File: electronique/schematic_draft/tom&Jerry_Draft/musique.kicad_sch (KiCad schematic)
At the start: 10 parts, among them U601 PAM8302AAY

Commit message: KiCAD V3 - 18.09.2024
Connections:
- net DAC STM32 renamed DAC_STM+
- net DAC_STM+: no longer C604.1
- new net DAC_STM-: C604.1
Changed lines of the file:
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@@
 		)
 	)
-	(global_label "HP+"
+	(hierarchical_label "HP+"
 		(shape input)
 		(at 167.64 81.28 0)
@@
 			(justify left)
 		)
-		(property "Intersheetrefs" "${INTERSHEET_REFS}"
-			(at 174.7981 81.28 0)
-			(effects
-				(font
-					(size 1.27 1.27)
-				)
-				(justify left)
-				(hide yes)
+	)
+	(hierarchical_label "HP-"
+		(shape input)
+		(at 167.64 99.06 0)
+		(fields_autoplaced yes)
+		(effects
+			(font
+				(size 1.27 1.27)
 			)
+			(justify left)
 		)
 	)
-	(global_label "DAC STM32"
+	(hierarchical_label "DAC_STM+"
 		(shape input)
 		(at 110.49 86.36 180)
@@
 			(justify right)
 		)
-		(property "Intersheetrefs" "${INTERSHEET_REFS}"
-			(at 96.8611 86.36 0)
-			(effects
-				(font
-					(size 1.27 1.27)
-				)
-				(justify right)
-				(hide yes)
-			)
-		)
 	)
-	(global_label "HP-"
-		(shape input)
-		(at 167.64 99.06 0)
-		(fields_autoplaced yes)
-		(effects
-			(font
-				(size 1.27 1.27)
-			)
-			(justify left)
-		)
-		(property "Intersheetrefs" "${INTERSHEET_REFS}"
-			(at 174.7981 99.06 0)
-			(effects
-				(font
-					(size 1.27 1.27)
-				)
-				(justify left)
-				(hide yes)
-			)
-		)
-	)
-	(global_label "DAC STM32"
+	(hierarchical_label "DAC_STM-"
 		(shape input)
 		(at 110.49 91.44 180)
@@
 			(justify right)
 		)
-		(property "Intersheetrefs" "${INTERSHEET_REFS}"
-			(at 96.8611 91.44 0)
-			(effects
-				(font
-					(size 1.27 1.27)
-				)
-				(justify right)
-				(hide yes)
-			)
-		)
 	)

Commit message: STM32 KiCAD V5 - 20.09.2024
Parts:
- added J601: Conn_01x02, symbol Connector_Generic:Conn_01x02
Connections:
- net HP+: now also J601.1 (Pin_1)
- net HP-: now also J601.2 (Pin_2)
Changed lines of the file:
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@@
 	)
 	(junction
-		(at 165.1 99.06)
+		(at 165.1 100.33)
 		(diameter 0)
 		(color 0 0 0 0)
@@
 	(wire
 		(pts
-			(xy 165.1 81.28) (xy 167.64 81.28)
+			(xy 165.1 81.28) (xy 190.5 81.28)
+		)
+		(stroke
+			(width 0)
+			(type default)
+		)
+	)
+	(wire
+		(pts
+			(xy 190.5 88.9) (xy 190.5 100.33)
 		)
 		(stroke
@@
 	(wire
 		(pts
+			(xy 190.5 81.28) (xy 190.5 86.36)
+		)
+		(stroke
+			(width 0)
+			(type default)
+		)
+	)
+	(wire
+		(pts
 			(xy 110.49 96.52) (xy 120.65 96.52)
 		)
@@
 	(wire
 		(pts
-			(xy 165.1 99.06) (xy 167.64 99.06)
+			(xy 165.1 100.33) (xy 190.5 100.33)
 		)
 		(stroke
@@
 		)
 	)
-	(hierarchical_label "HP+"
-		(shape input)
-		(at 167.64 81.28 0)
+	(label "HP-"
+		(at 190.5 93.98 0)
 		(fields_autoplaced yes)
 		(effects
@@
 				(size 1.27 1.27)
 			)
-			(justify left)
-		)
-	)
-	(hierarchical_label "HP-"
-		(shape input)
-		(at 167.64 99.06 0)
+			(justify left bottom)
+		)
+	)
+	(label "HP+"
+		(at 190.5 83.82 0)
 		(fields_autoplaced yes)
 		(effects
@@
 				(size 1.27 1.27)
 			)
-			(justify left)
+			(justify left bottom)
 		)
 	)
@@
 					(unit 1)
 				)
+			)
+		)
+	)
+	(symbol
+		(lib_id "Connector_Generic:Conn_01x02")
+		(at 195.58 86.36 0)
+		(unit 1)
+		(exclude_from_sim no)
+		(in_bom yes)
+		(on_board yes)
+		(dnp no)
+		(fields_autoplaced yes)
+		(property "Reference" "J601"
+			(at 198.12 86.3599 0)
+			(effects
+				(font
+					(size 1.27 1.27)
+				)
+				(justify left)
+			)
+		)
+		(property "Value" "Conn_01x02"
+			(at 198.12 88.8999 0)
+			(effects
+				(font
+					(size 1.27 1.27)
+				)
+				(justify left)
+			)
+		)
+		(property "Footprint" ""
+			(at 195.58 86.36 0)
+			(effects
+				(font
+					(size 1.27 1.27)
+				)
+				(hide yes)
+			)
+		)
+		(property "Datasheet" "~"
+			(at 195.58 86.36 0)
+			(effects
+				(font
+					(size 1.27 1.27)
+				)
+				(hide yes)
+			)
+		)
+		(property "Description" "Generic connector, single row, 01x02, script generated (kicad-library-utils/schlib/autogen/connector/)"
+			(at 195.58 86.36 0)
+			(effects
+				(font
+					(size 1.27 1.27)
+				)
+				(hide yes)
+			)
+		)
+		(pin "1"
+		)
+		(pin "2"
+		)
+		(instances
+			(project "tom&Jerry_Draft"
+				(path "/d6e3fbeb-d028-494d-83bf-2e4a8b12578d/8f8d8816-c3bc-4641-b521-76532fa599d5"
+					(reference "J601")
+					(unit 1)
+				)

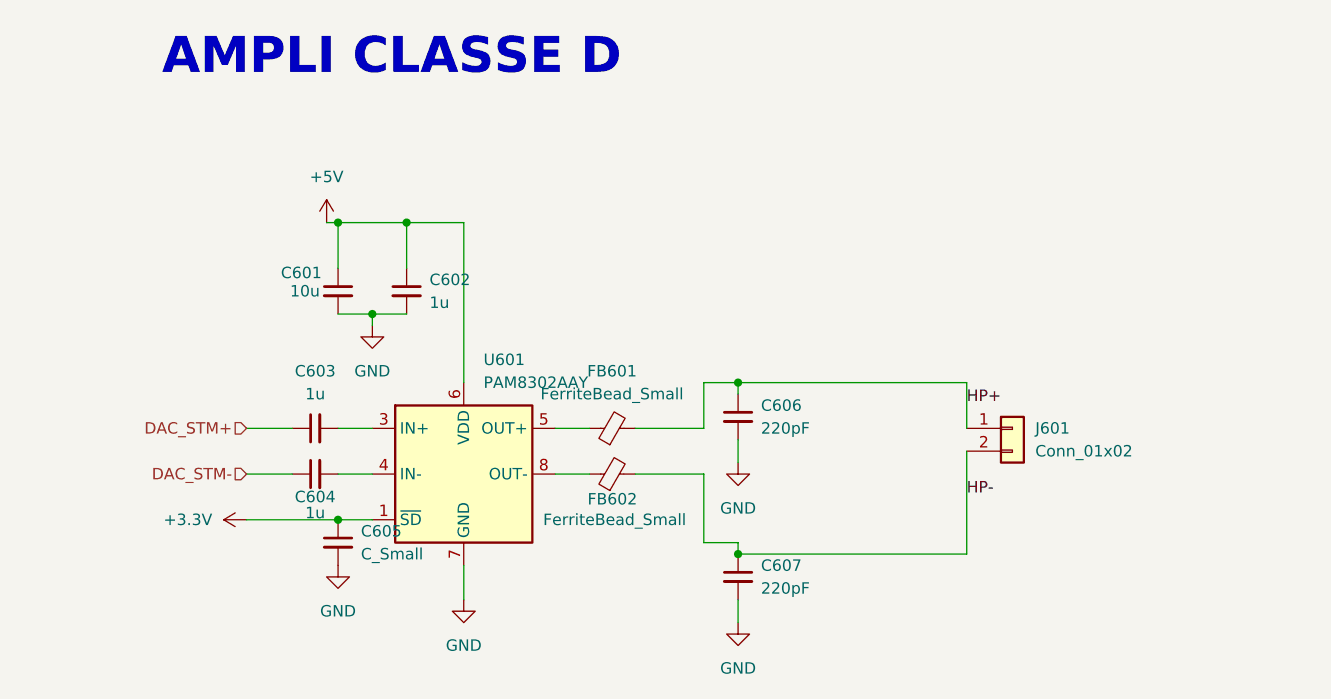
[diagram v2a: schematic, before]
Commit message: STM32 KiCAD V5 - 25.09.2024 - Ajout connecteurs TOF, ...
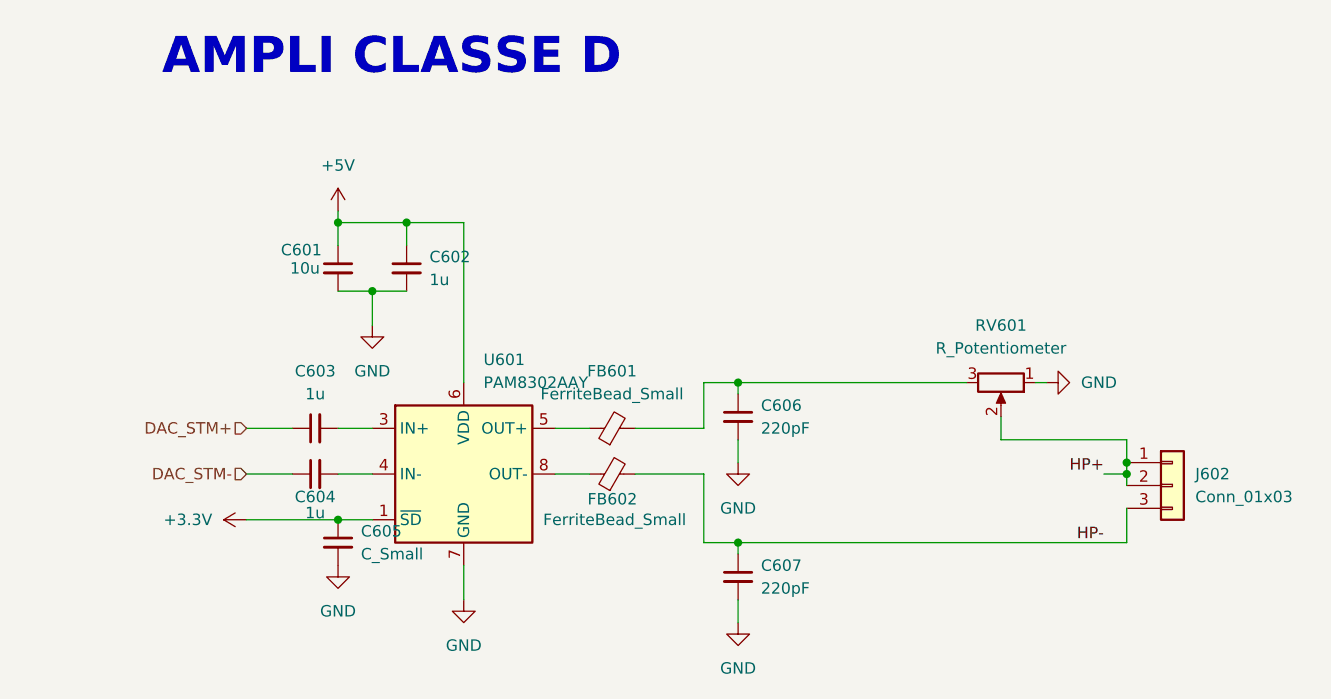
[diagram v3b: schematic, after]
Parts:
- removed J601: Conn_01x02, symbol Connector_Generic:Conn_01x02
- added J602: Conn_01x03, symbol Connector_Generic:Conn_01x03
- added RV601: R_Potentiometer, symbol Device:R_Potentiometer
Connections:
- net GND: now also RV601.1
- net HP+: now also J602.1 (Pin_1), J602.2 (Pin_2), RV601.2; no longer C606.1, FB601.2
- net HP-: now also J602.3 (Pin_3)
- new net: C606.1, FB601.2, RV601.3
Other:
- moved on the sheet: C601, C602

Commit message: STM32 KiCAD v2.0 x CubeIDE - Pin definitif + schematic reviewed
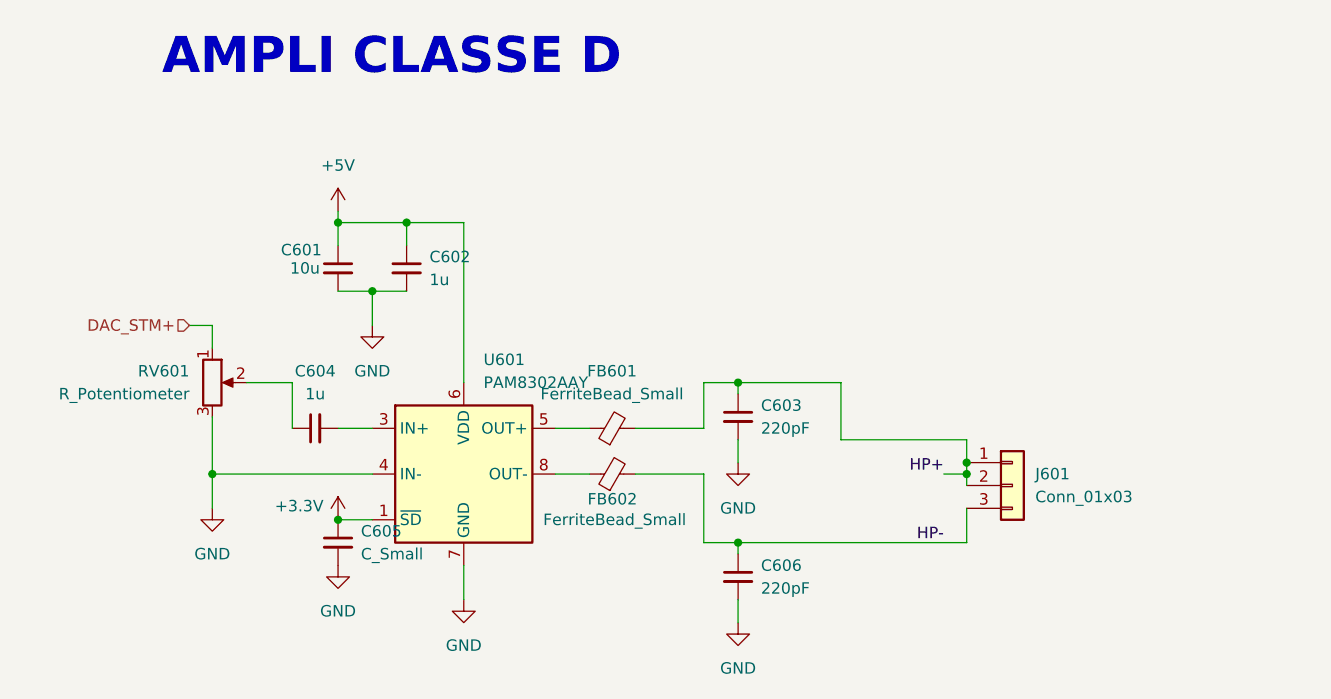
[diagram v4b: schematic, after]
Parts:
- removed C604: 1u, symbol Device:C_Small
- renumbered C606 to C603, C603 to C604, C607 to C606, J602 to J601
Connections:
- net DAC_STM+: now also RV601.1; no longer C604.1
- net GND: now also RV601.3, U601.4 (IN-); no longer RV601.1
- net HP+: now also C603.1, FB601.2; no longer RV601.2
- new net: C604.1, RV601.2
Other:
- moved on the sheet: J601

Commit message: Adding footprint V0.1
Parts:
- C601, C602, C604: footprint (none) -> Capacitor_SMD:C_0603_1608Metric
- C603, C606: value 220pF -> 220p; footprint (none) -> Capacitor_SMD:C_0402_1005Metric
- C605: value C_Small -> 100n; footprint (none) -> Capacitor_SMD:C_0402_1005Metric
- FB601, FB602: footprint (none) -> Inductor_SMD:L_0805_2012Metric
- J601: footprint (none) -> Connector_JST:JST_XH_S3B-XH-A_1x03_P2.50mm_Horizontal
- U601: footprint Package_DFN_QFN:DFN-8-1EP_3x3mm_P0.65mm_EP1.55x2.4mm -> Tom&Jerry:DFN300X300X80-8N
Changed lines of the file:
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@@
 			)
 		)
-		(property "Footprint" ""
+		(property "Footprint" "Capacitor_SMD:C_0603_1608Metric"
 			(at 118.11 86.36 0)
 			(effects
@@
 			)
 		)
-		(property "Value" "220pF"
+		(property "Value" "220p"
 			(at 167.64 104.1462 0)
 			(effects
@@
 			)
 		)
-		(property "Footprint" ""
+		(property "Footprint" "Capacitor_SMD:C_0402_1005Metric"
 			(at 165.1 102.87 0)
 			(effects
@@
 			)
 		)
-		(property "Value" "220pF"
+		(property "Value" "220p"
 			(at 167.64 86.3662 0)
 			(effects
@@
 			)
 		)
-		(property "Footprint" ""
+		(property "Footprint" "Capacitor_SMD:C_0402_1005Metric"
 			(at 165.1 85.09 0)
 			(effects
@@
 			)
 		)
-		(property "Footprint" ""
+		(property "Footprint" "Capacitor_SMD:C_0603_1608Metric"
 			(at 128.27 68.58 0)
 			(effects
@@
 			)
 		)
-		(property "Footprint" ""
+		(property "Footprint" "Connector_JST:JST_XH_S3B-XH-A_1x03_P2.50mm_Horizontal"
 			(at 195.58 92.71 0)
 			(effects
@@
 			)
 		)
-		(property "Footprint" "Package_DFN_QFN:DFN-8-1EP_3x3mm_P0.65mm_EP1.55x2.4mm"
+		(property "Footprint" "Tom&Jerry:DFN300X300X80-8N"
 			(at 134.62 91.44 0)
 			(effects
@@
 			)
 		)
-		(property "Footprint" ""
+		(property "Footprint" "Inductor_SMD:L_0805_2012Metric"
 			(at 151.13 88.138 90)
 			(effects
@@
 			)
 		)
-		(property "Footprint" ""
+		(property "Footprint" "Capacitor_SMD:C_0603_1608Metric"
 			(at 120.65 68.58 0)
 			(effects
@@
 			)
 		)
-		(property "Value" "C_Small"
+		(property "Value" "100n"
 			(at 123.19 100.3362 0)
 			(effects
@@
 			)
 		)
-		(property "Footprint" ""
+		(property "Footprint" "Capacitor_SMD:C_0402_1005Metric"
 			(at 120.65 99.06 0)
 			(effects
@@
 			)
 		)
-		(property "Footprint" ""
+		(property "Footprint" "Inductor_SMD:L_0805_2012Metric"
 			(at 151.13 93.218 90)
 			(effects

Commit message: Ajout V2 TOF + MultiPCB Panalize
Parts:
- renumbered C604 to C601, C601 to C602, C605 to C603, C602 to C604, C603 to C605
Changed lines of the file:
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@@
 		(dnp no)
 		(fields_autoplaced yes)
-		(property "Reference" "C604"
+		(property "Reference" "C601"
 			(at 118.1163 80.01 90)
 			(effects
@@
 			(project "tom&Jerry_Draft"
 				(path "/d6e3fbeb-d028-494d-83bf-2e4a8b12578d/8f8d8816-c3bc-4641-b521-76532fa599d5"
-					(reference "C604")
+					(reference "C601")
 					(unit 1)
 				)
@@
 		(dnp no)
 		(fields_autoplaced yes)
-		(property "Reference" "C603"
+		(property "Reference" "C605"
 			(at 167.64 83.8262 0)
 			(effects
@@
 			(project ""
 				(path "/d6e3fbeb-d028-494d-83bf-2e4a8b12578d/8f8d8816-c3bc-4641-b521-76532fa599d5"
-					(reference "C603")
+					(reference "C605")
 					(unit 1)
 				)
@@
 		(dnp no)
 		(fields_autoplaced yes)
-		(property "Reference" "C602"
+		(property "Reference" "C604"
 			(at 130.81 67.3162 0)
 			(effects
@@
 			(project "tom&Jerry_Draft"
 				(path "/d6e3fbeb-d028-494d-83bf-2e4a8b12578d/8f8d8816-c3bc-4641-b521-76532fa599d5"
-					(reference "C602")
+					(reference "C604")
 					(unit 1)
 				)
@@
 		(dnp no)
 		(fields_autoplaced yes)
-		(property "Reference" "#PWR0607"
+		(property "Reference" "#PWR0606"
 			(at 134.62 111.76 0)
 			(effects
@@
 			(project "tom&Jerry_Draft"
 				(path "/d6e3fbeb-d028-494d-83bf-2e4a8b12578d/8f8d8816-c3bc-4641-b521-76532fa599d5"
-					(reference "#PWR0607")
+					(reference "#PWR0606")
 					(unit 1)
 				)
@@
 		(on_board yes)
 		(dnp no)
-		(property "Reference" "#PWR0605"
+		(property "Reference" "#PWR0603"
 			(at 120.65 100.33 0)
 			(effects
@@
 			(project ""
 				(path "/d6e3fbeb-d028-494d-83bf-2e4a8b12578d/8f8d8816-c3bc-4641-b521-76532fa599d5"
-					(reference "#PWR0605")
+					(reference "#PWR0603")
 					(unit 1)
 				)
@@
 		(dnp no)
 		(fields_autoplaced yes)
-		(property "Reference" "#PWR0601"
+		(property "Reference" "#PWR0602"
 			(at 120.65 66.04 0)
 			(effects
@@
 			(project "tom&Jerry_Draft"
 				(path "/d6e3fbeb-d028-494d-83bf-2e4a8b12578d/8f8d8816-c3bc-4641-b521-76532fa599d5"
-					(reference "#PWR0601")
+					(reference "#PWR0602")
 					(unit 1)
 				)
@@
 		(dnp no)
 		(fields_autoplaced yes)
-		(property "Reference" "#PWR0606"
+		(property "Reference" "#PWR0604"
 			(at 120.65 107.95 0)
 			(effects
@@
 			(project ""
 				(path "/d6e3fbeb-d028-494d-83bf-2e4a8b12578d/8f8d8816-c3bc-4641-b521-76532fa599d5"
-					(reference "#PWR0606")
+					(reference "#PWR0604")
 					(unit 1)
 				)
@@
 		(dnp no)
 		(fields_autoplaced yes)
-		(property "Reference" "#PWR0603"
+		(property "Reference" "#PWR0607"
 			(at 165.1 96.52 0)
 			(effects
@@
 			(project "tom&Jerry_Draft"
 				(path "/d6e3fbeb-d028-494d-83bf-2e4a8b12578d/8f8d8816-c3bc-4641-b521-76532fa599d5"
-					(reference "#PWR0603")
+					(reference "#PWR0607")
 					(unit 1)
 				)
@@
 		(dnp no)
 		(fields_autoplaced yes)
-		(property "Reference" "#PWR0602"
+		(property "Reference" "#PWR0605"
 			(at 124.46 81.28 0)
 			(effects
@@
 			(project "tom&Jerry_Draft"
 				(path "/d6e3fbeb-d028-494d-83bf-2e4a8b12578d/8f8d8816-c3bc-4641-b521-76532fa599d5"
-					(reference "#PWR0602")
+					(reference "#PWR0605")
 					(unit 1)
 				)
@@
 		(on_board yes)
 		(dnp no)
-		(property "Reference" "C601"
+		(property "Reference" "C602"
 			(at 114.3 66.548 0)
 			(effects
@@
 			(project "tom&Jerry_Draft"
 				(path "/d6e3fbeb-d028-494d-83bf-2e4a8b12578d/8f8d8816-c3bc-4641-b521-76532fa599d5"
-					(reference "C601")
+					(reference "C602")
 					(unit 1)
 				)
@@
 		(dnp no)
 		(fields_autoplaced yes)
-		(property "Reference" "C605"
+		(property "Reference" "C603"
 			(at 123.19 97.7962 0)
 			(effects
@@
 			(project ""
 				(path "/d6e3fbeb-d028-494d-83bf-2e4a8b12578d/8f8d8816-c3bc-4641-b521-76532fa599d5"
-					(reference "C605")
+					(reference "C603")
 					(unit 1)
 				)
@@
 		(dnp no)
 		(fields_autoplaced yes)
-		(property "Reference" "#PWR0604"
+		(property "Reference" "#PWR0601"
 			(at 106.68 101.6 0)
 			(effects
@@
 			(project ""
 				(path "/d6e3fbeb-d028-494d-83bf-2e4a8b12578d/8f8d8816-c3bc-4641-b521-76532fa599d5"
-					(reference "#PWR0604")
-					(unit 1)
-				)
+					(reference "#PWR0601")
+					(unit 1)
+				)

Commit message: V2.0 placement avec tout dessus
Aucun routage réalisé
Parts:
- RV601: footprint (none) -> Tom&Jerry:Potar
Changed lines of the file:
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@@
 			)
 		)
-		(property "Footprint" ""
+		(property "Footprint" "Tom&Jerry:Potar"
 			(at 106.68 81.28 0)
 			(effects

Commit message: Routage Signal Complet - PCB V2.0
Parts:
- renumbered C602 to C601, C604 to C602, C605 to C603, C601 to C604, C603 to C605
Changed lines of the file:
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@@
 		(dnp no)
 		(fields_autoplaced yes)
-		(property "Reference" "C601"
+		(property "Reference" "C604"
 			(at 118.1163 80.01 90)
 			(effects
@@
 			(project "tom&Jerry_Draft"
 				(path "/d6e3fbeb-d028-494d-83bf-2e4a8b12578d/8f8d8816-c3bc-4641-b521-76532fa599d5"
-					(reference "C601")
+					(reference "C604")
 					(unit 1)
 				)
@@
 		(dnp no)
 		(fields_autoplaced yes)
-		(property "Reference" "C605"
+		(property "Reference" "C603"
 			(at 167.64 83.8262 0)
 			(effects
@@
 			(project ""
 				(path "/d6e3fbeb-d028-494d-83bf-2e4a8b12578d/8f8d8816-c3bc-4641-b521-76532fa599d5"
-					(reference "C605")
+					(reference "C603")
 					(unit 1)
 				)
@@
 		(dnp no)
 		(fields_autoplaced yes)
-		(property "Reference" "C604"
+		(property "Reference" "C602"
 			(at 130.81 67.3162 0)
 			(effects
@@
 			(project "tom&Jerry_Draft"
 				(path "/d6e3fbeb-d028-494d-83bf-2e4a8b12578d/8f8d8816-c3bc-4641-b521-76532fa599d5"
-					(reference "C604")
+					(reference "C602")
 					(unit 1)
 				)
@@
 		(dnp no)
 		(fields_autoplaced yes)
-		(property "Reference" "#PWR0606"
+		(property "Reference" "#PWR0607"
 			(at 134.62 111.76 0)
 			(effects
@@
 			(project "tom&Jerry_Draft"
 				(path "/d6e3fbeb-d028-494d-83bf-2e4a8b12578d/8f8d8816-c3bc-4641-b521-76532fa599d5"
-					(reference "#PWR0606")
+					(reference "#PWR0607")
 					(unit 1)
 				)
@@
 		(on_board yes)
 		(dnp no)
-		(property "Reference" "#PWR0603"
+		(property "Reference" "#PWR0605"
 			(at 120.65 100.33 0)
 			(effects
@@
 			(project ""
 				(path "/d6e3fbeb-d028-494d-83bf-2e4a8b12578d/8f8d8816-c3bc-4641-b521-76532fa599d5"
-					(reference "#PWR0603")
+					(reference "#PWR0605")
 					(unit 1)
 				)
@@
 		(dnp no)
 		(fields_autoplaced yes)
-		(property "Reference" "#PWR0602"
+		(property "Reference" "#PWR0601"
 			(at 120.65 66.04 0)
 			(effects
@@
 			(project "tom&Jerry_Draft"
 				(path "/d6e3fbeb-d028-494d-83bf-2e4a8b12578d/8f8d8816-c3bc-4641-b521-76532fa599d5"
-					(reference "#PWR0602")
+					(reference "#PWR0601")
 					(unit 1)
 				)
@@
 		(dnp no)
 		(fields_autoplaced yes)
-		(property "Reference" "#PWR0604"
+		(property "Reference" "#PWR0606"
 			(at 120.65 107.95 0)
 			(effects
@@
 			(project ""
 				(path "/d6e3fbeb-d028-494d-83bf-2e4a8b12578d/8f8d8816-c3bc-4641-b521-76532fa599d5"
-					(reference "#PWR0604")
+					(reference "#PWR0606")
 					(unit 1)
 				)
@@
 		(dnp no)
 		(fields_autoplaced yes)
-		(property "Reference" "#PWR0607"
+		(property "Reference" "#PWR0603"
 			(at 165.1 96.52 0)
 			(effects
@@
 			(project "tom&Jerry_Draft"
 				(path "/d6e3fbeb-d028-494d-83bf-2e4a8b12578d/8f8d8816-c3bc-4641-b521-76532fa599d5"
-					(reference "#PWR0607")
+					(reference "#PWR0603")
 					(unit 1)
 				)
@@
 		(dnp no)
 		(fields_autoplaced yes)
-		(property "Reference" "#PWR0605"
+		(property "Reference" "#PWR0602"
 			(at 124.46 81.28 0)
 			(effects
@@
 			(project "tom&Jerry_Draft"
 				(path "/d6e3fbeb-d028-494d-83bf-2e4a8b12578d/8f8d8816-c3bc-4641-b521-76532fa599d5"
-					(reference "#PWR0605")
+					(reference "#PWR0602")
 					(unit 1)
 				)
@@
 		(on_board yes)
 		(dnp no)
-		(property "Reference" "C602"
+		(property "Reference" "C601"
 			(at 114.3 66.548 0)
 			(effects
@@
 			(project "tom&Jerry_Draft"
 				(path "/d6e3fbeb-d028-494d-83bf-2e4a8b12578d/8f8d8816-c3bc-4641-b521-76532fa599d5"
-					(reference "C602")
+					(reference "C601")
 					(unit 1)
 				)
@@
 		(dnp no)
 		(fields_autoplaced yes)
-		(property "Reference" "C603"
+		(property "Reference" "C605"
 			(at 123.19 97.7962 0)
 			(effects
@@
 			(project ""
 				(path "/d6e3fbeb-d028-494d-83bf-2e4a8b12578d/8f8d8816-c3bc-4641-b521-76532fa599d5"
-					(reference "C603")
+					(reference "C605")
 					(unit 1)
 				)
@@
 		(dnp no)
 		(fields_autoplaced yes)
-		(property "Reference" "#PWR0601"
+		(property "Reference" "#PWR0604"
 			(at 106.68 101.6 0)
 			(effects
@@
 			(project ""
 				(path "/d6e3fbeb-d028-494d-83bf-2e4a8b12578d/8f8d8816-c3bc-4641-b521-76532fa599d5"
-					(reference "#PWR0601")
-					(unit 1)
-				)
+					(reference "#PWR0604")
+					(unit 1)
+				)
